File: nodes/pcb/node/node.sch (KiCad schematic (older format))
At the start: 33 parts, among them J1 Other Hemisphere, J2 FTDI Basic, J3 Burner, J4 Port, J5 Port, J6 Other Hemisphere, J7 Port, J8 Port, U1 MIC5205YM5, U2 ATmega328P-AU, U3 LP2985-3.3, U4 ADXL335, Y1 16MHz

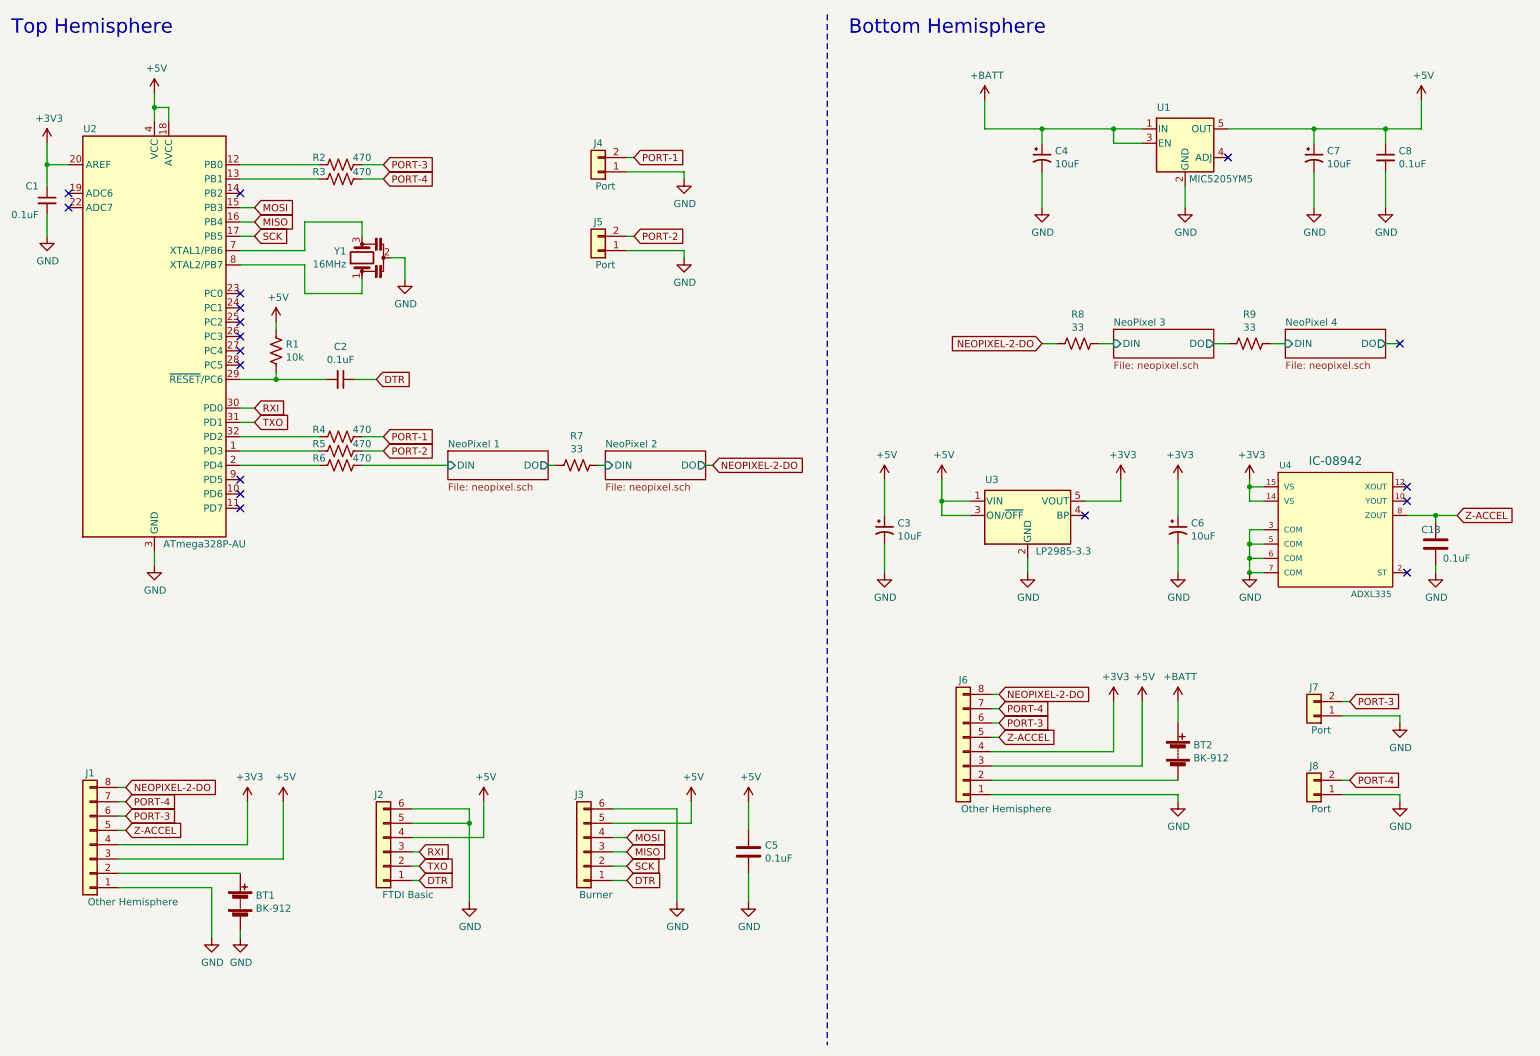
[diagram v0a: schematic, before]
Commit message: Fix ERC errors (except for 2 which can be ignored)
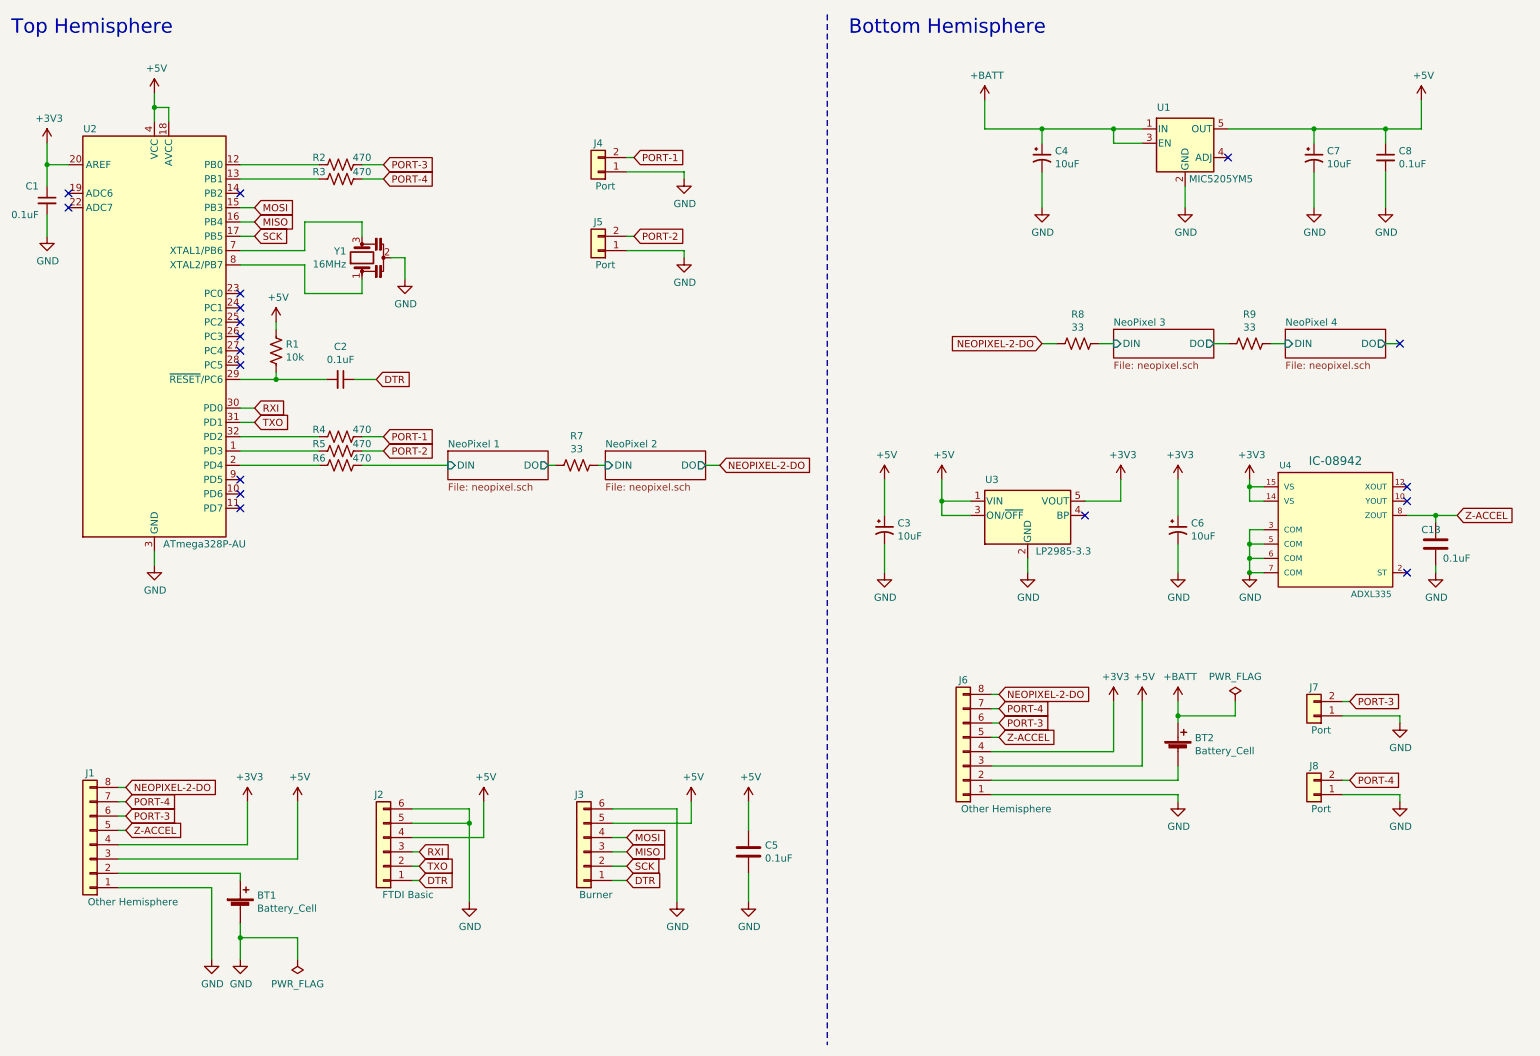
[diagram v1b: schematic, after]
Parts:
- removed BT1, BT2: BK-912, SnapEDA:BAT_BK-913-TR, symbol Device:Battery
- added BT1, BT2: Battery_Cell, Common-Parts-Library:MPD_BK-912-TR, symbol Device:Battery_Cell
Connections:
- net +BATT: now also BT2.1 (+)
- net GND: now also BT1.2 (-)
- net at J1.2 (Pin_2): now also BT1.1 (+)
- net at J6.2 (Pin_2): now also BT2.2 (-)
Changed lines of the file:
@@
-	1    0    0    -1
-$EndComp
-$Comp
-L Device:C C5
-U 1 1 5C7EEDE3
-P 5750 6400
-F 0 "C5" H 5865 6446 50  0000 L CNN
-F 1 "0.1uF" H 5865 6355 50  0000 L CNN
-F 2 "Capacitor_SMD:C_0603_1608Metric_Pad1.05x0.95mm_HandSolder" H 5788 6250 50  0001 C CNN
-F 3 "~" H 5750 6400 50  0001 C CNN
-	1    5750 6400
 	1    0    0    -1
 $EndComp
@@
 	4800 6600 4900 6600
 $Comp
-L Device:Battery BT1
-U 1 1 5C81AC66
-P 2200 6750
-F 0 "BT1" H 2308 6796 50  0000 L CNN
-F 1 "BK-912" H 2308 6705 50  0000 L CNN
-F 2 "SnapEDA:BAT_BK-913-TR" V 2200 6810 50  0001 C CNN
-F 3 "http://www.memoryprotectiondevices.com/datasheets/BK-912-datasheet.pdf" V 2200 6810 50  0001 C CNN
-	1    2200 6750
-	1    0    0    -1
-$EndComp
-$Comp
 L power:GND #PWR0118
 U 1 1 5C81AF18
-P 2200 7000
-F 0 "#PWR0118" H 2200 6750 50  0001 C CNN
-F 1 "GND" H 2205 6827 50  0000 C CNN
-F 2 "" H 2200 7000 50  0001 C CNN
-F 3 "" H 2200 7000 50  0001 C CNN
-	1    2200 7000
+P 2200 7150
+F 0 "#PWR0118" H 2200 6900 50  0001 C CNN
+F 1 "GND" H 2205 6977 50  0000 C CNN
+F 2 "" H 2200 7150 50  0001 C CNN
+F 3 "" H 2200 7150 50  0001 C CNN
+	1    2200 7150
 	1    0    0    -1
 $EndComp
@@
 L power:GND #PWR0119
 U 1 1 5C85E55F
-P 2000 7000
-F 0 "#PWR0119" H 2000 6750 50  0001 C CNN
-F 1 "GND" H 2005 6827 50  0000 C CNN
-F 2 "" H 2000 7000 50  0001 C CNN
-F 3 "" H 2000 7000 50  0001 C CNN
-	1    2000 7000
+P 2000 7150
+F 0 "#PWR0119" H 2000 6900 50  0001 C CNN
+F 1 "GND" H 2005 6977 50  0000 C CNN
+F 2 "" H 2000 7150 50  0001 C CNN
+F 3 "" H 2000 7150 50  0001 C CNN
+	1    2000 7150
 	1    0    0    -1
 $EndComp
@@
 	1350 6650 2000 6650
 Wire Wire Line
-	2000 6650 2000 7000
+	2000 6650 2000 7150
 Wire Wire Line
 	1350 6550 2200 6550
-$Comp
-L Device:Battery BT2
-U 1 1 5C8658D9
-P 8750 5700
-F 0 "BT2" H 8858 5746 50  0000 L CNN
-F 1 "BK-912" H 8858 5655 50  0000 L CNN
-F 2 "SnapEDA:BAT_BK-913-TR" V 8750 5760 50  0001 C CNN
-F 3 "http://www.memoryprotectiondevices.com/datasheets/BK-912-datasheet.pdf" V 8750 5760 50  0001 C CNN
-	1    8750 5700
-	1    0    0    -1
-$EndComp
-Wire Wire Line
-	1350 6450 2500 6450
-Wire Wire Line
-	2500 6450 2500 6050
+Wire Wire Line
+	1350 6450 2600 6450
+Wire Wire Line
+	2600 6450 2600 6050
 Text GLabel 1400 6150 2    50   Input ~ 0
 PORT-3
@@
 	4700 3700 4750 3700
 Wire Wire Line
-	5450 3700 5500 3700
-Text GLabel 5500 3700 2    50   Input ~ 0
+	5450 3700 5550 3700
+Text GLabel 5550 3700 2    50   Input ~ 0
 NEOPIXEL-2-DO
 Text GLabel 7800 2850 0    50   Input ~ 0
@@
 L power:+5V #PWR0116
 U 1 1 5CD9B0CE
-P 2500 6050
-F 0 "#PWR0116" H 2500 5900 50  0001 C CNN
-F 1 "+5V" H 2515 6223 50  0000 C CNN
-F 2 "" H 2500 6050 50  0001 C CNN
-F 3 "" H 2500 6050 50  0001 C CNN
-	1    2500 6050
+P 2600 6050
+F 0 "#PWR0116" H 2600 5900 50  0001 C CNN
+F 1 "+5V" H 2615 6223 50  0000 C CNN
+F 2 "" H 2600 6050 50  0001 C CNN
+F 3 "" H 2600 6050 50  0001 C CNN
+	1    2600 6050
 	1    0    0    -1
 $EndComp
@@
 Wire Wire Line
 	8800 1900 8800 1750
-Wire Wire Line
-	2200 7000 2200 6950
 Wire Wire Line
 	6700 3800 6700 4050
@@
 	3350 2250 3250 2250
 Wire Wire Line
-	8750 5350 8750 5500
+	8750 5350 8750 5450
 $Comp
 L power:+BATT #PWR0152
@@
 	1    0    0    -1
 $EndComp
+$Comp
+L Device:C C5
+U 1 1 5C7EEDE3
+P 5750 6400
+F 0 "C5" H 5865 6446 50  0000 L CNN
+F 1 "0.1uF" H 5865 6355 50  0000 L CNN
+F 2 "Capacitor_SMD:C_0603_1608Metric_Pad1.05x0.95mm_HandSolder" H 5788 6250 50  0001 C CNN
+F 3 "~" H 5750 6400 50  0001 C CNN
+	1    5750 6400
+	1    0    0    -1
+$EndComp
+$Comp
+L Device:Battery_Cell BT1
+U 1 1 5C8E9BC5
+P 2200 6800
+F 0 "BT1" H 2318 6896 50  0000 L CNN
+F 1 "Battery_Cell" H 2318 6805 50  0000 L CNN
+F 2 "Common-Parts-Library:MPD_BK-912-TR" V 2200 6860 50  0001 C CNN
+F 3 "~" V 2200 6860 50  0001 C CNN
+	1    2200 6800
+	1    0    0    -1
+$EndComp
+$Comp
+L Device:Battery_Cell BT2
+U 1 1 5C8E9CBF
+P 8750 5700
+F 0 "BT2" H 8868 5796 50  0000 L CNN
+F 1 "Battery_Cell" H 8868 5705 50  0000 L CNN
+F 2 "Common-Parts-Library:MPD_BK-912-TR" V 8750 5760 50  0001 C CNN
+F 3 "~" V 8750 5760 50  0001 C CNN
+	1    8750 5700
+	1    0    0    -1
+$EndComp
+Wire Wire Line
+	8750 5800 8750 5900
+Wire Wire Line
+	2200 6550 2200 6600
+Wire Wire Line
+	2200 6900 2200 7000
+$Comp
+L power:PWR_FLAG #FLG0105
+U 1 1 5C90E0B0
+P 9150 5350
+F 0 "#FLG0105" H 9150 5425 50  0001 C CNN
+F 1 "PWR_FLAG" H 9150 5524 50  0000 C CNN
+F 2 "" H 9150 5350 50  0001 C CNN
+F 3 "~" H 9150 5350 50  0001 C CNN
+	1    9150 5350
+	1    0    0    -1
+$EndComp
+Wire Wire Line
+	9150 5350 9150 5450
+Wire Wire Line
+	9150 5450 8750 5450
+Connection ~ 8750 5450
+Wire Wire Line
+	8750 5450 8750 5500
+$Comp
+L power:PWR_FLAG #FLG0106
+U 1 1 5C91A6DA
+P 2600 7150
+F 0 "#FLG0106" H 2600 7225 50  0001 C CNN
+F 1 "PWR_FLAG" H 2600 7323 50  0000 C CNN
+F 2 "" H 2600 7150 50  0001 C CNN
+F 3 "~" H 2600 7150 50  0001 C CNN
+	1    2600 7150
+	-1   0    0    1
+$EndComp
+Wire Wire Line
+	2200 7000 2600 7000
+Wire Wire Line
+	2600 7000 2600 7150
+Connection ~ 2200 7000
+Wire Wire Line
+	2200 7000 2200 7150
 $EndSCHEMATC

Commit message: Rearrange
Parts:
- J1: value Other Hemisphere -> Top Hemisphere
- J6: value Other Hemisphere -> Bottom Hemisphere
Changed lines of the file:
@@
 P 7250 5700
 F 0 "J6" H 7250 5200 50  0000 C CNN
-F 1 "Other Hemisphere" H 6950 6100 50  0000 C CNN
+F 1 "Bottom Hemisphere" H 6900 6100 50  0000 C CNN
 F 2 "Connector_PinHeader_2.54mm:PinHeader_2x04_P2.54mm_Vertical" H 7250 5700 50  0001 C CNN
 F 3 "~" H 7250 5700 50  0001 C CNN
@@
 P 1150 6350
 F 0 "J1" H 1150 5850 50  0000 C CNN
-F 1 "Other Hemisphere" H 850 6750 50  0000 C CNN
+F 1 "Top Hemisphere" H 850 6750 50  0000 C CNN
 F 2 "Connector_PinHeader_2.54mm:PinHeader_2x04_P2.54mm_Vertical" H 1150 6350 50  0001 C CNN
 F 3 "~" H 1150 6350 50  0001 C CNN
